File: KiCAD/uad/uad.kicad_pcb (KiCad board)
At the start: 2 copper layers, 50 x 50 mm, 32 parts

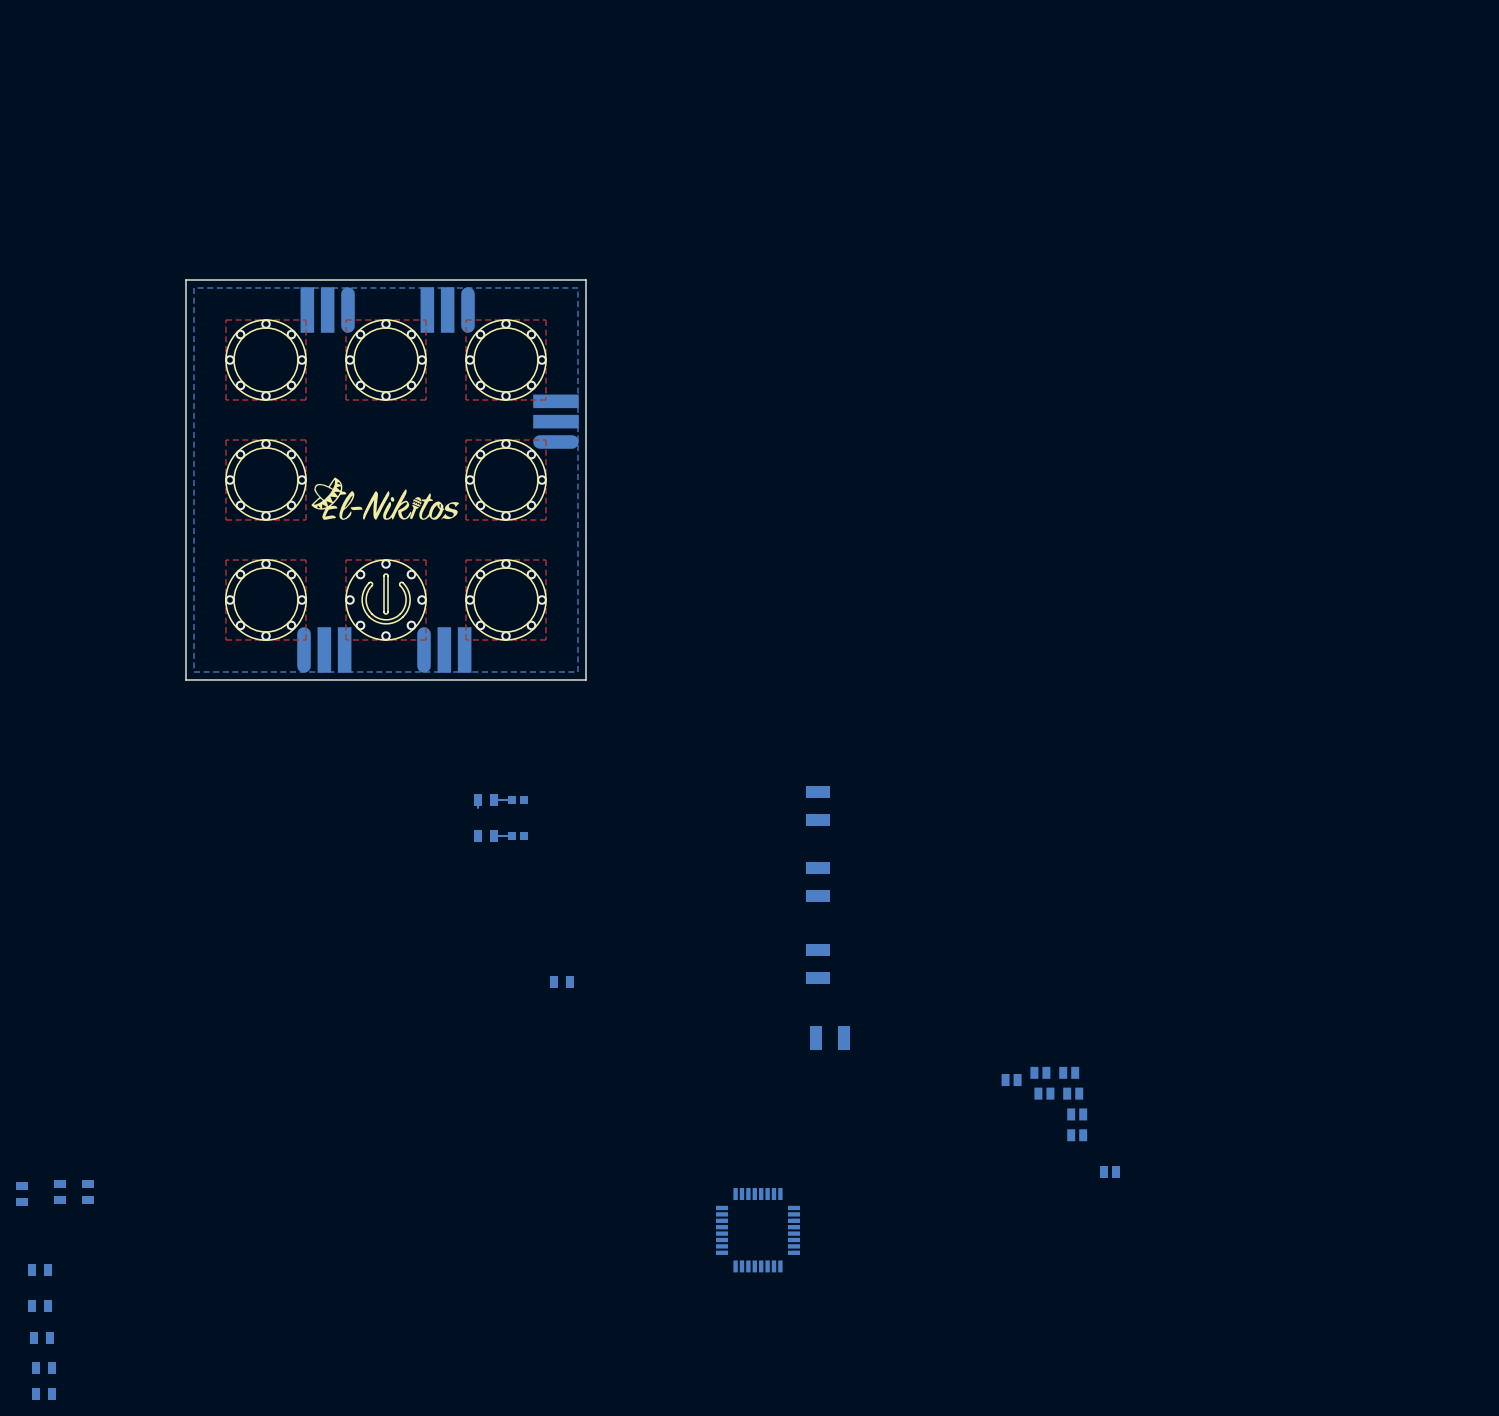
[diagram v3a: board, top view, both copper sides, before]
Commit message: разведена плата кнопок, плата контроллера - не расставлены светодиоды
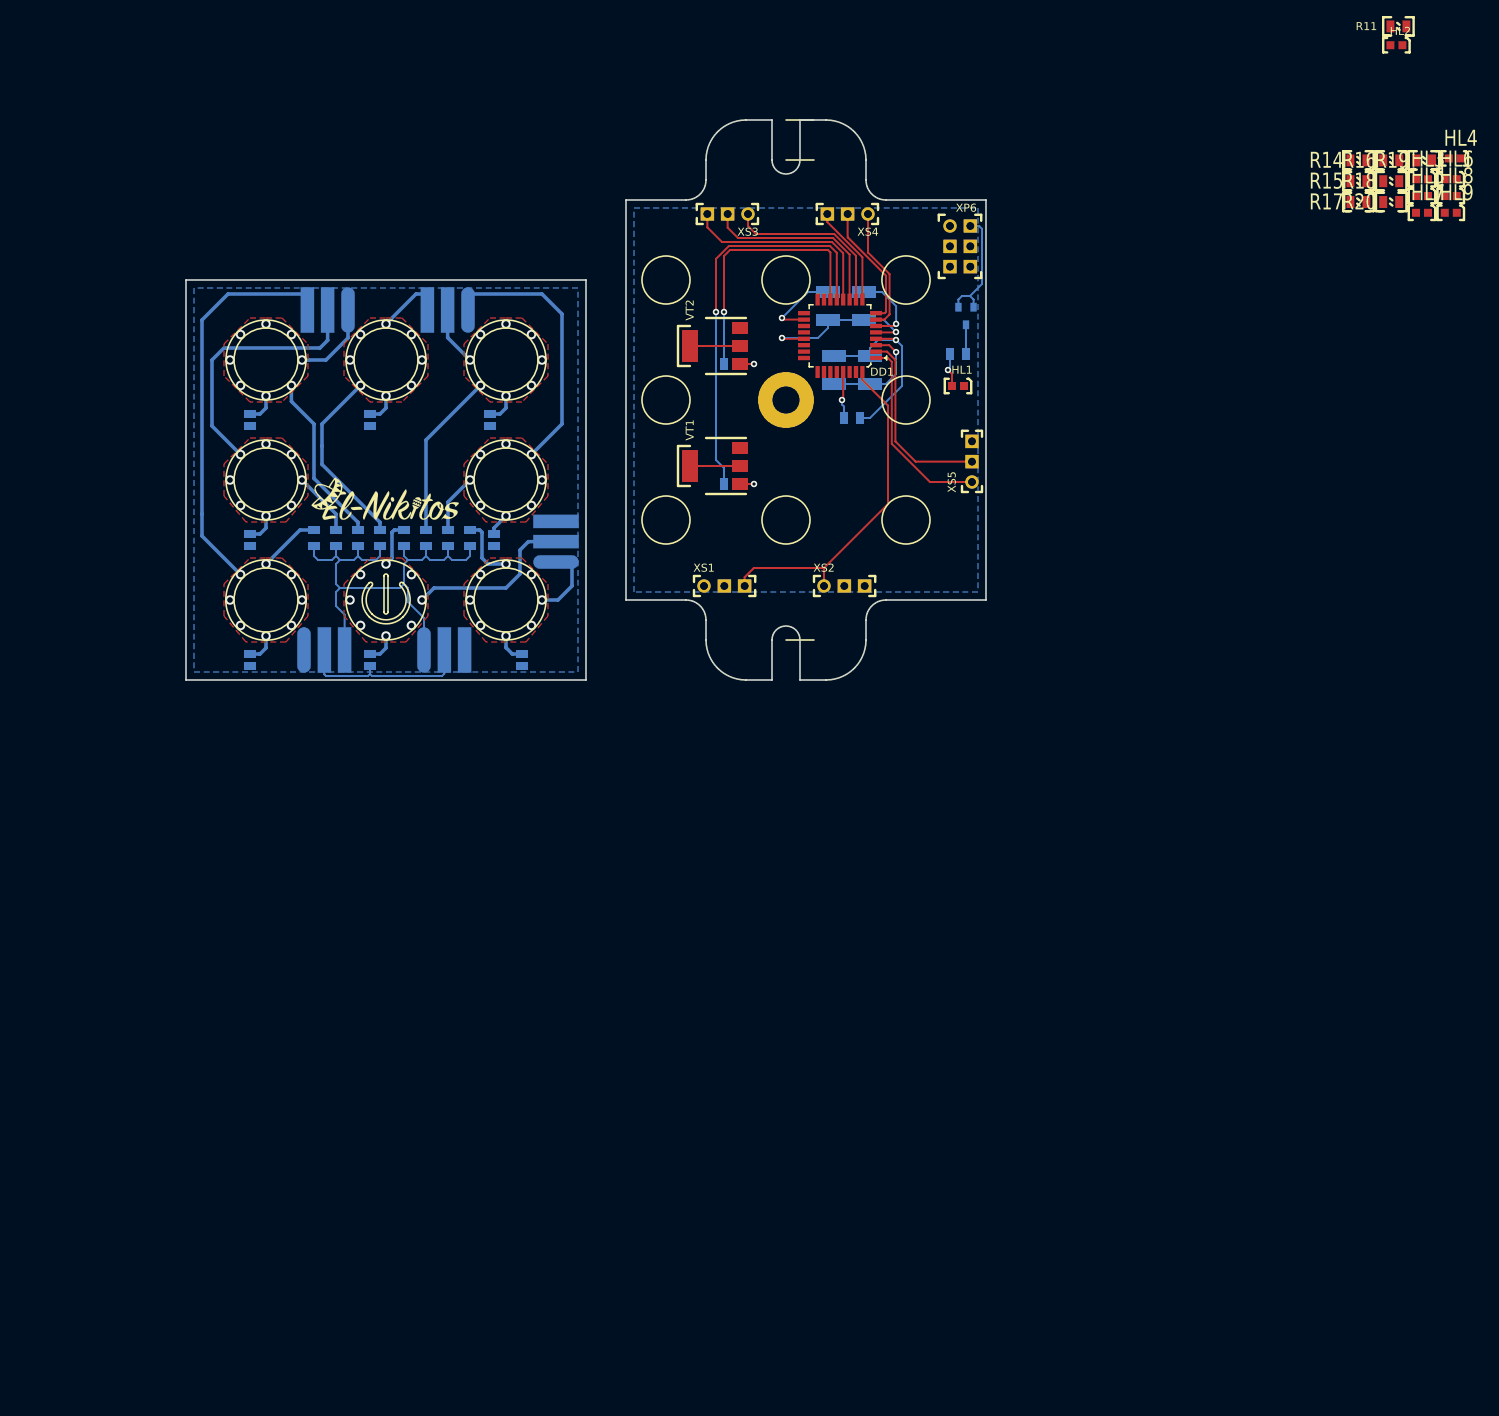
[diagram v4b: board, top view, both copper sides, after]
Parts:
- added HL3: Светодиод, N_VD_HL:Светодиод_SMD_0603, F.Cu at (224.0, 85.4)
- added HL4: Светодиод, N_VD_HL:Светодиод_SMD_0603, F.Cu at (228.1, 82.8)
- added HL5: Светодиод, N_VD_HL:Светодиод_SMD_0603, F.Cu at (224.0, 87.5)
- added HL6: Светодиод, N_VD_HL:Светодиод_SMD_0603, F.Cu at (227.6, 85.4)
- added HL7: Светодиод, N_VD_HL:Светодиод_SMD_0603, F.Cu at (224.0, 89.6)
- added HL8: Светодиод, N_VD_HL:Светодиод_SMD_0603, F.Cu at (227.6, 87.5)
- added HL9: Светодиод, N_VD_HL:Светодиод_SMD_0603, F.Cu at (227.6, 89.6)
- added M3: ОтверстиеD3, N_X:ОтверстиеD3, F.Cu at (145.2, 113.0)
- added R12: 300 Ом(0805), N_RLC:Резистор_SMD_0805_0,125Вт, B.Cu at (139.5, 123.5)
- added R13: 300 Ом(0805), N_RLC:Резистор_SMD_0805_0,125Вт, B.Cu at (139.5, 108.5)
- added R14: 100 Ом(0805), N_RLC:Резистор_SMD_0805_0,125Вт, F.Cu at (215.8, 83.1)
- added R15: 100 Ом(0805), N_RLC:Резистор_SMD_0805_0,125Вт, F.Cu at (215.8, 85.7)
- added R16: 100 Ом(0805), N_RLC:Резистор_SMD_0805_0,125Вт, F.Cu at (219.9, 83.1)
- added R17: 100 Ом(0805), N_RLC:Резистор_SMD_0805_0,125Вт, F.Cu at (215.8, 88.3)
- added R18: 100 Ом(0805), N_RLC:Резистор_SMD_0805_0,125Вт, F.Cu at (219.9, 85.7)
- added R19: 100 Ом(0805), N_RLC:Резистор_SMD_0805_0,125Вт, F.Cu at (224.0, 83.1)
- added R20: 100 Ом(0805), N_RLC:Резистор_SMD_0805_0,125Вт, F.Cu at (219.9, 88.3)
- added VD1: Диод_шоттки, N_VD_HL:Диод_BAR43CFILM_SOT-23, B.Cu at (167.8, 102.5)
- added VT1: PBSS4540Z, N_VD_HL:Транзистор_NPN_SOT223, F.Cu at (135.8, 121.2)
- added VT2: PBSS4540Z, N_VD_HL:Транзистор_NPN_SOT223, F.Cu at (135.8, 106.2)
- added XP6: Вилка_PLD6_ПРОГ, N_X:Вилка_PLD6_вертикальная, F.Cu at (165.8, 91.2)
- added XS1: Розетка_PBS3, N_X:Розетка_PBS3_вертикальная, F.Cu at (135.0, 136.2)
- added XS2: Розетка_PBS3, N_X:Розетка_PBS3_вертикальная, F.Cu at (150.0, 136.2)
- added XS3: Розетка_PBS3, N_X:Розетка_PBS3_вертикальная, F.Cu at (140.5, 89.8)
- added XS4: Розетка_PBS3, N_X:Розетка_PBS3_вертикальная, F.Cu at (155.5, 89.8)
- added XS5: Розетка_PBS3, N_X:Розетка_PBS3_вертикальная, F.Cu at (168.5, 123.2)
- DD1, HL1, HL2, R11: moved to F.Cu
- moved R11 152.5 mm to (220.8, 66.3)
- moved HL2 147.7 mm to (220.8, 68.7)
- moved C4 127.1 mm to (78.2, 116.2), turned to 90 degrees
- moved C3 123.0 mm to (78.2, 131.2), turned to 90 degrees
- moved C5 122.8 mm to (93.2, 116.2), turned to 90 degrees
- moved R8 119.1 mm to (105.8, 131.2), turned to 90 degrees
- moved R7 114.9 mm to (103.0, 131.2), turned to 90 degrees
- moved C2 113.7 mm to (78.2, 146.2), turned to 90 degrees
- moved C1 111.4 mm to (93.2, 146.2), turned to 90 degrees
- moved R6 110.5 mm to (100.2, 131.2), turned to 90 degrees
- moved C6 108.0 mm to (108.2, 116.2), turned to 90 degrees
- moved DD1 106.7 mm to (156.2, 107.8)
- moved R5 104.5 mm to (94.5, 131.2), turned to 90 degrees
- moved C7 103.1 mm to (108.8, 131.2), turned to 90 degrees
- moved R4 99.3 mm to (91.8, 131.2), turned to 90 degrees
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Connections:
- net GND renamed /uab_logic/GND
- net LED_work renamed /uab_logic/LED_1
- net RES renamed /uab_logic/RES
- net RX renamed /uab_logic/RX
- net TX renamed /uab_logic/TX
- net VCC renamed /uab_logic/VCC
- DD1 pad 1: Net-(DD1-Pad1) -> /uab_logic/BUT_8_IN
- DD1 pad 10: Net-(DD1-Pad10) -> /uab_logic/BUT_4_IN
- DD1 pad 11: Net-(DD1-Pad11) -> /uab_logic/BUT_3_IN
- DD1 pad 12: Net-(DD1-Pad12) -> /uab_logic/BUT_2_IN
- DD1 pad 13: PWM_OUT_1 -> /uab_logic/PWM_OUT_1
- DD1 pad 14: PWM_OUT_2 -> /uab_logic/PWM_OUT_2
- DD1 pad 15: MOSI -> /uab_logic/MOSI
- DD1 pad 16: MISO -> /uab_logic/MISO
- DD1 pad 17: SCK -> /uab_logic/SCK
- DD1 pad 2: Net-(DD1-Pad2) -> /uab_logic/BUT_1_IN
- DD1 pad 32: Net-(DD1-Pad32) -> /uab_logic/BUT_COM_OUT
- DD1 pad 7: Net-(DD1-Pad7) -> /uab_logic/BUT_7_IN
- DD1 pad 8: Net-(DD1-Pad8) -> /uab_logic/BUT_6_IN
- DD1 pad 9: Net-(DD1-Pad9) -> /uab_logic/BUT_5_IN
- XP1 pad 1: /uad_sensor/BUT_COM_OUT -> /uad_sensor/GND
- XP1 pad 3: /uad_sensor/GND -> /uad_sensor/BUT_COM_OUT
- XP2 pad 1: /uad_sensor/GND -> /uad_sensor/BUT_COM_OUT
- XP2 pad 3: /uad_sensor/BUT_COM_OUT -> /uad_sensor/GND
- XP3 pad 1: /uad_sensor/BUT_1_CUP -> /uad_sensor/BUT_4_CUP
- XP3 pad 2: /uad_sensor/BUT_2_CUP -> /uad_sensor/BUT_3_CUP
- XP3 pad 3: /uad_sensor/BUT_3_CUP -> /uad_sensor/BUT_2_CUP
- XP4 pad 1: /uad_sensor/BUT_4_CUP -> /uad_sensor/BUT_7_CUP
- XP4 pad 2: /uad_sensor/BUT_5_CUP -> /uad_sensor/BUT_6_CUP
- XP4 pad 3: /uad_sensor/BUT_6_CUP -> /uad_sensor/BUT_5_CUP
- XP5 pad 1: /uad_sensor/BUT_7_CUP -> /uad_sensor/BUT_8_CUP
- XP5 pad 2: /uad_sensor/BUT_8_CUP -> /uad_sensor/BUT_1_CUP
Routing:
- net /uad_sensor/BUT_COM_OUT: track 0.00 -> 66.0 mm
- net /uad_sensor/BUT_2_CUP: track 0.00 -> 59.9 mm
- net /uab_logic/PWM_OUT_1: track 0.00 -> 50.8 mm, vias 0 -> 1
- net /uab_logic/VCC: track 1.00 -> 47.9 mm, vias 1 -> 3
- net /uad_sensor/BUT_3_CUP: track 0.00 -> 46.4 mm, vias 9 -> 8
- net /uab_logic/BUT_COM_OUT: track 0.00 -> 42.9 mm
- net /uad_sensor/BUT_7_CUP: track 0.00 -> 42.2 mm, vias 4 -> 8
- net /uad_sensor/BUT_4_CUP: track 0.00 -> 37.7 mm, vias 9 -> 8
- net /uab_logic/PWM_OUT_2: track 0.00 -> 34.9 mm, vias 0 -> 1
- net /uab_logic/GND: track 0.00 -> 34.8 mm, vias 0 -> 3
- net /uad_sensor/BUT_6_CUP: track 0.00 -> 34.1 mm, vias 0 -> 8
- net /uad_sensor/BUT_1_CUP: track 0.00 -> 34.1 mm, vias 7 -> 8
- net /uad_sensor/BUT_5_CUP: track 0.00 -> 33.6 mm, vias 7 -> 8
- net /uab_logic/BUT_2_IN: track 0.00 -> 25.8 mm
- net /uab_logic/BUT_8_IN: track 0.00 -> 24.4 mm
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- added copper zone on B.Cu, net /uad_sensor/GND
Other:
- board size 50 x 50 mm -> 100 x 70 mm

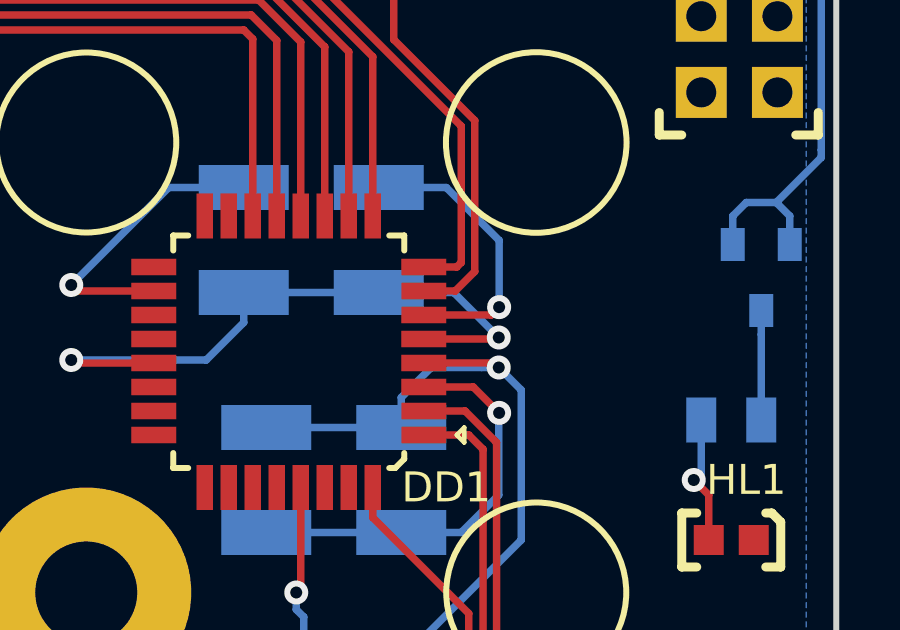
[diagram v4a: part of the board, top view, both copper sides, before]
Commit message: начато добавление клеммников на схему
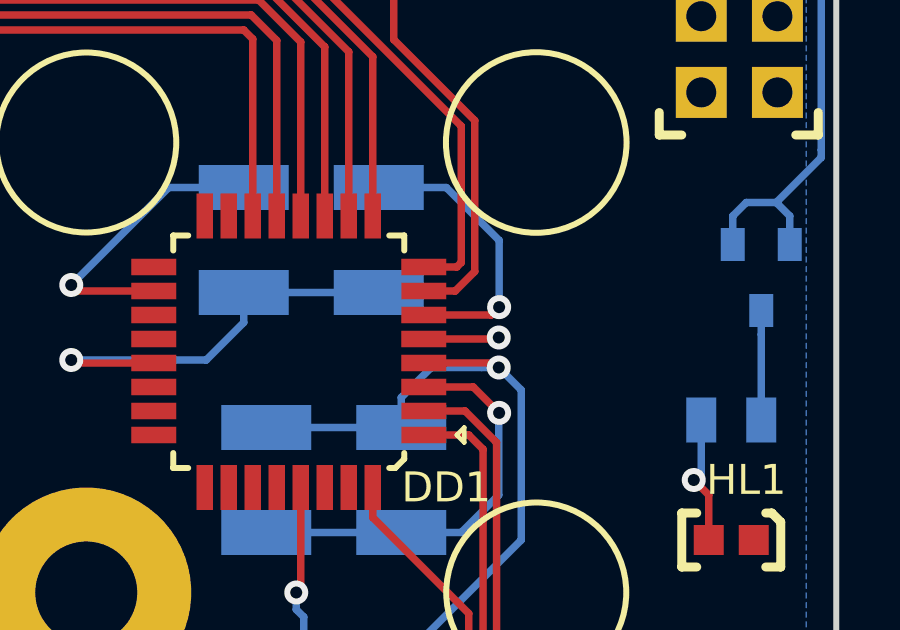
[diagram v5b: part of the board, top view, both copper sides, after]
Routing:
- net /uab_logic/GND: track 34.8 -> 31.0 mm
